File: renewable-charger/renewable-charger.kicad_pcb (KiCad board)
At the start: 2 copper layers, 149.9 x 41.9 mm, 31 parts, among them J1 Solar Input, J2 Wind Output, J3 Output, M1 Stepper_Motor_bipolar, Q1 P-channel 30V 4A MOSfet, U1 CN3791

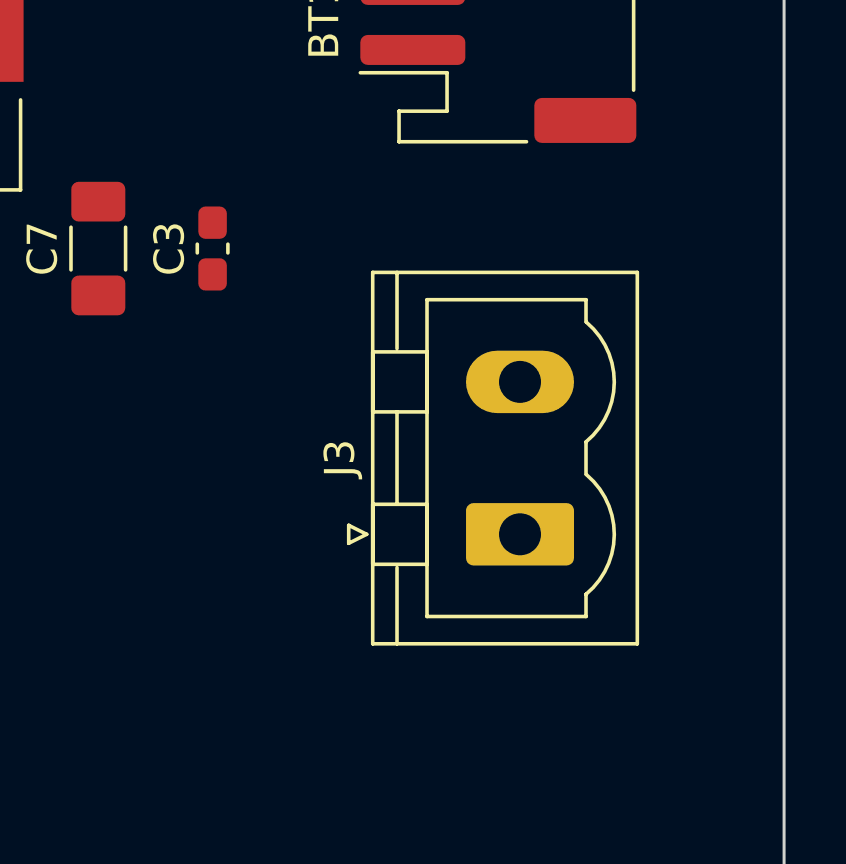
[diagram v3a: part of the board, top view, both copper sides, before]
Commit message: Add test point to measure current into the battery.  Implements #8
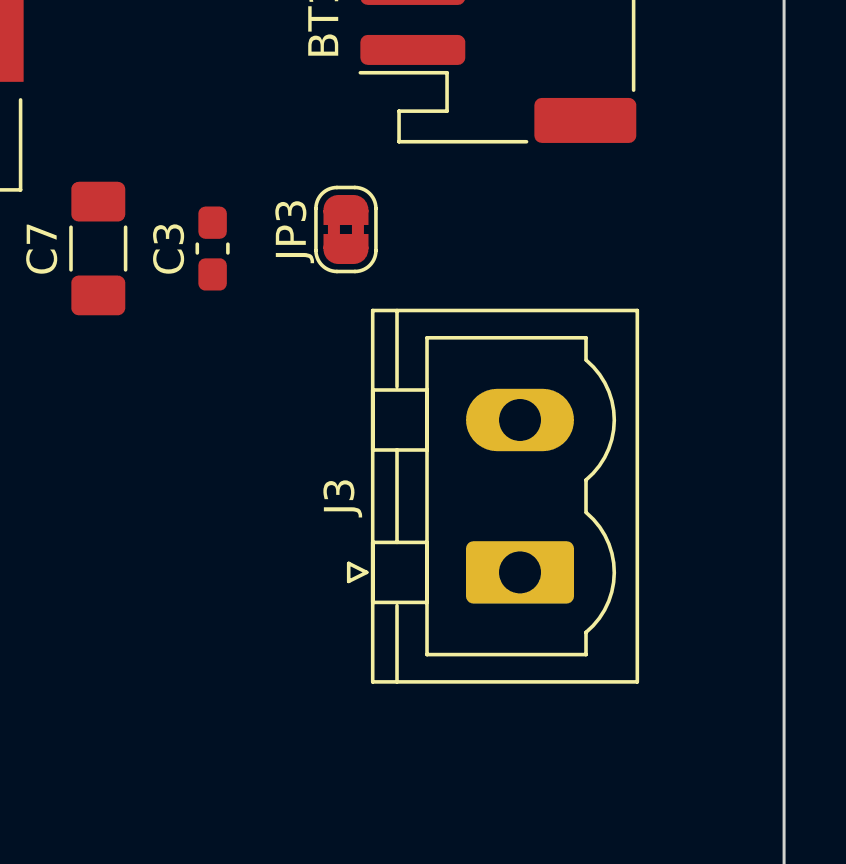
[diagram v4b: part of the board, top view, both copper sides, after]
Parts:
- added JP3: Test Point, Jumper:SolderJumper-2_P1.3mm_Bridged2Bar_RoundedPad1.0x1.5mm, F.Cu at (247.7, 77.5)
- moved J3 1.27 mm to (253.5, 88.9)
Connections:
- C3 pad 1: Net-(BT1-+) -> Net-(J3-Pin_1)
- C7 pad 1: Net-(BT1-+) -> Net-(J3-Pin_1)
- J3 pad 1: Net-(BT1-+) -> Net-(J3-Pin_1)
- R5 pad 2: Net-(BT1-+) -> Net-(J3-Pin_1)
- U1 pad 7: Net-(BT1-+) -> Net-(J3-Pin_1)
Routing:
- net Net-(J3-Pin_1): track 0.00 -> 14.2 mm
- net Net-(BT1-+): track 14.2 -> 0.00 mm
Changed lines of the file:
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@@
   (net 19 "Net-(M1--)")
   (net 20 "Net-(JP2-A)")
+  (net 21 "Net-(J3-Pin_1)")
   (footprint "Resistor_SMD:R_0805_2012Metric_Pad1.20x1.40mm_HandSolder" (layer "F.Cu")
     (at 230.505 78.74 -90)
@@
       (net 11 "Net-(U1-CSP)") (pintype "passive"))
     (pad "2" smd roundrect (at 1 0 270) (size 1.2 1.4) (layers "F.Cu" "F.Paste" "F.Mask") (roundrect_rratio 0.208333)
-      (net 1 "Net-(BT1-+)") (pintype "passive"))
+      (net 21 "Net-(J3-Pin_1)") (pintype "passive"))
     (model "${KICAD6_3DMODEL_DIR}/Resistor_SMD.3dshapes/R_0805_2012Metric.wrl"
       (offset (xyz 0 0 0))
@@
   )
   (footprint "Connector_Phoenix_MSTB:PhoenixContact_MSTBVA_2,5_2-G-5,08_1x02_P5.08mm_Vertical" (layer "F.Cu")
-    (at 253.4525 87.63 90)
+    (at 253.4525 88.9 90)
     (descr "Generic Phoenix Contact connector footprint for: MSTBVA_2,5/2-G-5,08; number of pins: 02; pin pitch: 5.08mm; Vertical || order number: 1755736 12A || order number: 1924305 16A (HC)")
     (tags "phoenix_contact connector MSTBVA_01x02_G_5.08mm")
@@
       (stroke (width 0.1) (type solid)) (layer "F.Fab"))
     (pad "1" thru_hole roundrect (at 0 0 90) (size 2.08 3.6) (drill 1.4) (layers *.Cu *.Mask) (roundrect_rratio 0.120192)
-      (net 1 "Net-(BT1-+)") (pinfunction "Pin_1") (pintype "passive"))
+      (net 21 "Net-(J3-Pin_1)") (pinfunction "Pin_1") (pintype "passive"))
     (pad "2" thru_hole oval (at 5.08 0 90) (size 2.08 3.6) (drill 1.4) (layers *.Cu *.Mask)
       (net 2 "/Power -") (pinfunction "Pin_2") (pintype "passive"))
@@
       (stroke (width 0.1) (type solid)) (layer "F.Fab"))
     (pad "1" smd roundrect (at -0.8625 0 90) (size 1.075 0.95) (layers "F.Cu" "F.Paste" "F.Mask") (roundrect_rratio 0.25)
-      (net 1 "Net-(BT1-+)") (pintype "passive"))
+      (net 21 "Net-(J3-Pin_1)") (pintype "passive"))
     (pad "2" smd roundrect (at 0.8625 0 90) (size 1.075 0.95) (layers "F.Cu" "F.Paste" "F.Mask") (roundrect_rratio 0.25)
       (net 2 "/Power -") (pintype "passive"))
@@
     )
   )
+  (footprint "Jumper:SolderJumper-2_P1.3mm_Bridged2Bar_RoundedPad1.0x1.5mm" (layer "F.Cu")
+    (at 247.65 77.47 90)
+    (descr "SMD Solder Jumper, 1x1.5mm, rounded Pads, 0.3mm gap, bridged with 2 copper strips")
+    (tags "net tie solder jumper bridged")
+    (property "Sheetfile" "renewable-charger.kicad_sch")
+    (property "Sheetname" "")
+    (attr exclude_from_pos_files)
+    (fp_text reference "JP3" (at 0 -1.8 90) (layer "F.SilkS")
+      (effects (font (size 1 1) (thickness 0.15)))
+    )
+    (fp_text value "Test Point" (at 0 1.9 90) (layer "F.Fab")
+      (effects (font (size 1 1) (thickness 0.15)))
+    )
+    (fp_poly
+      (pts
+        (xy -0.25 -0.6)
+        (xy 0.25 -0.6)
+        (xy 0.25 -0.2)
+        (xy -0.25 -0.2)
+      )
+      (stroke (width 0) (type solid)) (fill solid) (layer "F.Cu"))
+    (fp_poly
+      (pts
+        (xy -0.25 0.2)
+        (xy 0.25 0.2)
+        (xy 0.25 0.6)
+        (xy -0.25 0.6)
+      )
+      (stroke (width 0) (type solid)) (fill solid) (layer "F.Cu"))
+    (fp_line (start -1.4 0.3) (end -1.4 -0.3)
+      (stroke (width 0.12) (type solid)) (layer "F.SilkS"))
+    (fp_line (start -0.7 -1) (end 0.7 -1)
+      (stroke (width 0.12) (type solid)) (layer "F.SilkS"))
+    (fp_line (start 0.7 1) (end -0.7 1)
+      (stroke (width 0.12) (type solid)) (layer "F.SilkS"))
+    (fp_line (start 1.4 -0.3) (end 1.4 0.3)
+      (stroke (width 0.12) (type solid)) (layer "F.SilkS"))
+    (fp_arc (start -1.4 -0.3) (mid -1.194975 -0.794975) (end -0.7 -1)
+      (stroke (width 0.12) (type solid)) (layer "F.SilkS"))
+    (fp_arc (start -0.7 1) (mid -1.194975 0.794975) (end -1.4 0.3)
+      (stroke (width 0.12) (type solid)) (layer "F.SilkS"))
+    (fp_arc (start 0.7 -1) (mid 1.194975 -0.794975) (end 1.4 -0.3)
+      (stroke (width 0.12) (type solid)) (layer "F.SilkS"))
+    (fp_arc (start 1.4 0.3) (mid 1.194975 0.794975) (end 0.7 1)
+      (stroke (width 0.12) (type solid)) (layer "F.SilkS"))
+    (fp_line (start -1.65 -1.25) (end -1.65 1.25)
+      (stroke (width 0.05) (type solid)) (layer "F.CrtYd"))
+    (fp_line (start -1.65 -1.25) (end 1.65 -1.25)
+      (stroke (width 0.05) (type solid)) (layer "F.CrtYd"))
+    (fp_line (start 1.65 1.25) (end -1.65 1.25)
+      (stroke (width 0.05) (type solid)) (layer "F.CrtYd"))
+    (fp_line (start 1.65 1.25) (end 1.65 -1.25)
+      (stroke (width 0.05) (type solid)) (layer "F.CrtYd"))
+    (pad "1" smd custom (at -0.65 0 90) (size 1 0.5) (layers "F.Cu" "F.Mask")
+      (net 21 "Net-(J3-Pin_1)") (pinfunction "A") (pintype "passive") (zone_connect 2) (thermal_bridge_angle 45)
+      (options (clearance outline) (anchor rect))
+      (primitives
+        (gr_circle (center 0 0.25) (end 0.5 0.25) (width 0) (fill yes))
+        (gr_circle (center 0 -0.25) (end 0.5 -0.25) (width 0) (fill yes))
+        (gr_poly
+          (pts
+            (xy 0.5 0.75)
+            (xy 0 0.75)
+            (xy 0 -0.75)
+            (xy 0.5 -0.75)
+          )
+ (width 0) (fill yes))
+      ))
+    (pad "2" smd custom (at 0.65 0 90) (size 1 0.5) (layers "F.Cu" "F.Mask")
+      (net 1 "Net-(BT1-+)") (pinfunction "B") (pintype "passive") (zone_connect 2) (thermal_bridge_angle 45)
+      (options (clearance outline) (anchor rect))
+      (primitives
+        (gr_circle (center 0 0.25) (end 0.5 0.25) (width 0) (fill yes))
+        (gr_circle (center 0 -0.25) (end 0.5 -0.25) (width 0) (fill yes))
+        (gr_poly
+          (pts
+            (xy 0 0.75)
+            (xy -0.5 0.75)
+            (xy -0.5 -0.75)
+            (xy 0 -0.75)
+          )
+ (width 0) (fill yes))
+      ))
+  )
   (footprint "Package_TO_SOT_SMD:SOT-23" (layer "F.Cu")
     (at 209.55 70.485)
@@
       (stroke (width 0.1) (type solid)) (layer "F.Fab"))
     (pad "1" smd roundrect (at -1.5625 0 90) (size 1.325 1.8) (layers "F.Cu" "F.Paste" "F.Mask") (roundrect_rratio 0.188679)
-      (net 1 "Net-(BT1-+)") (pintype "passive"))
+      (net 21 "Net-(J3-Pin_1)") (pintype "passive"))
     (pad "2" smd roundrect (at 1.5625 0 90) (size 1.325 1.8) (layers "F.Cu" "F.Paste" "F.Mask") (roundrect_rratio 0.188679)
       (net 2 "/Power -") (pintype "passive"))
@@
       (net 14 "Net-(U1-MPPT)") (pinfunction "MPPT") (pintype "input"))
     (pad "7" smd rect (at 2.55 1 90) (size 1.1 0.51) (layers "F.Cu" "F.Paste" "F.Mask")
-      (net 1 "Net-(BT1-+)") (pinfunction "BAT") (pintype "input"))
+      (net 21 "Net-(J3-Pin_1)") (pinfunction "BAT") (pintype "input"))
     (pad "8" smd rect (at 2.55 0 90) (size 1.1 0.51) (layers "F.Cu" "F.Paste" "F.Mask")
       (net 11 "Net-(U1-CSP)") (pinfunction "CSP") (pintype "input"))
@@
   (gr_rect (start 112.395 59.69) (end 262.255 101.6)
     (stroke (width 0.1) (type default)) (fill none) (layer "Edge.Cuts"))
-  (segment (start 219.44 76.19) (end 219.44 75.895) (width 0.25) (layer "F.Cu") (net 1))
-  (segment (start 221.364771 75.315489) (end 224.155 78.105718) (width 0.25) (layer "F.Cu") (net 1))
-  (segment (start 224.155 79.375) (end 224.52 79.74) (width 0.25) (layer "F.Cu") (net 1))
-  (segment (start 224.155 78.105718) (end 224.155 79.375) (width 0.25) (layer "F.Cu") (net 1))
-  (segment (start 220.019511 75.315489) (end 221.364771 75.315489) (width 0.25) (layer "F.Cu") (net 1))
-  (segment (start 224.52 79.74) (end 230.505 79.74) (width 0.25) (layer "F.Cu") (net 1))
-  (segment (start 219.44 75.895) (end 220.019511 75.315489) (width 0.25) (layer "F.Cu") (net 1))
   (segment (start 168.8 83.82) (end 168.8 75.04) (width 1.3) (layer "F.Cu") (net 2))
   (segment (start 129.06 71.91) (end 125.79 71.91) (width 1.3) (layer "F.Cu") (net 2))
@@
   (segment (start 163.195 67.31) (end 163.1075 67.2225) (width 0.25) (layer "F.Cu") (net 20))
   (segment (start 163.195 75.55) (end 163.195 67.31) (width 0.25) (layer "F.Cu") (net 20))
+  (segment (start 219.44 76.19) (end 219.44 75.895) (width 0.25) (layer "F.Cu") (net 21))
+  (segment (start 221.364771 75.315489) (end 224.155 78.105718) (width 0.25) (layer "F.Cu") (net 21))
+  (segment (start 224.155 79.375) (end 224.52 79.74) (width 0.25) (layer "F.Cu") (net 21))
+  (segment (start 224.155 78.105718) (end 224.155 79.375) (width 0.25) (layer "F.Cu") (net 21))
+  (segment (start 220.019511 75.315489) (end 221.364771 75.315489) (width 0.25) (layer "F.Cu") (net 21))
+  (segment (start 224.52 79.74) (end 230.505 79.74) (width 0.25) (layer "F.Cu") (net 21))
+  (segment (start 219.44 75.895) (end 220.019511 75.315489) (width 0.25) (layer "F.Cu") (net 21))
 )

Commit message: Add micro-USB connector for USB charging.  Implements #7
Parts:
- added J4: USB_B_Micro, Connector_USB:USB_Micro-B_Amphenol_10118194_Horizontal, F.Cu at (193.0, 89.5)
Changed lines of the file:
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@@
   (net 20 "Net-(JP2-A)")
   (net 21 "Net-(J3-Pin_1)")
+  (net 22 "unconnected-(J4-D-)")
+  (net 23 "unconnected-(J4-D+)")
+  (net 24 "unconnected-(J4-ID)")
+  (net 25 "unconnected-(J4-Shield)")
   (footprint "Resistor_SMD:R_0805_2012Metric_Pad1.20x1.40mm_HandSolder" (layer "F.Cu")
     (at 230.505 78.74 -90)
@@
       (offset (xyz 0 0 0))
       (scale (xyz 1 1 1))
+      (rotate (xyz 0 0 0))
+    )
+  )
+  (footprint "Connector_USB:USB_Micro-B_Amphenol_10118194_Horizontal" (layer "F.Cu")
+    (at 193.04 89.535)
+    (descr "USB Micro-B receptacle, horizontal, SMD, 10118194, https://cdn.amphenol-icc.com/media/wysiwyg/files/drawing/10118194.pdf")
+    (tags "USB Micro B horizontal SMD")
+    (property "Farnell" "2668482")
+    (property "Farnell Price/Stock" "https://uk.farnell.com/amphenol-icc-fci/10118194-0001lf/micro-usb-2-0-type-b-rcpt-smt/dp/2668482")
+    (property "Sheetfile" "renewable-charger.kicad_sch")
+    (property "Sheetname" "")
+    (attr smd)
+    (fp_text reference "J4" (at 0 -3.5) (layer "F.SilkS")
+      (effects (font (size 1 1) (thickness 0.15)))
+    )
+    (fp_text value "USB_B_Micro" (at 0 4.75) (layer "F.Fab")
+      (effects (font (size 1 1) (thickness 0.15)))
+    )
+    (fp_text user "PCB Edge" (at 0 2.75) (layer "Dwgs.User")
+      (effects (font (size 0.5 0.5) (thickness 0.08)))
+    )
+    (fp_text user "${REFERENCE}" (at 0 -0.05) (layer "F.Fab")
+      (effects (font (size 1 1) (thickness 0.15)))
+    )
+    (fp_line (start -3.76 -1.66) (end -3.34 -1.66)
+      (stroke (width 0.12) (type solid)) (layer "F.SilkS"))
+    (fp_line (start -3.76 0.32) (end -3.76 -1.66)
+      (stroke (width 0.12) (type solid)) (layer "F.SilkS"))
+    (fp_line (start -3.76 2.69) (end -3.76 2.29)
+      (stroke (width 0.12) (type solid)) (layer "F.SilkS"))
+    (fp_line (start -1.76 -1.89) (end -1.76 -2.34)
+      (stroke (width 0.12) (type solid)) (layer "F.SilkS"))
+    (fp_line (start -1.31 -2.34) (end -1.76 -2.34)
+      (stroke (width 0.12) (type solid)) (layer "F.SilkS"))
+    (fp_line (start 3.76 -1.66) (end 3.34 -1.66)
+      (stroke (width 0.12) (type solid)) (layer "F.SilkS"))
+    (fp_line (start 3.76 0.32) (end 3.76 -1.66)
+      (stroke (width 0.12) (type solid)) (layer "F.SilkS"))
+    (fp_line (start 3.76 2.29) (end 3.76 2.69)
+      (stroke (width 0.12) (type solid)) (layer "F.SilkS"))
+    (fp_line (start 3 2.75) (end -3 2.75)
+      (stroke (width 0.1) (type solid)) (layer "Dwgs.User"))
+    (fp_line (start -4.45 -2.58) (end -4.45 3.95)
+      (stroke (width 0.05) (type solid)) (layer "F.CrtYd"))
+    (fp_line (start -4.45 -2.58) (end 4.45 -2.58)
+      (stroke (width 0.05) (type solid)) (layer "F.CrtYd"))
+    (fp_line (start -4.45 3.95) (end 4.45 3.95)
+      (stroke (width 0.05) (type solid)) (layer "F.CrtYd"))
+    (fp_line (start 4.45 -2.58) (end 4.45 3.95)
+      (stroke (width 0.05) (type solid)) (layer "F.CrtYd"))
+    (fp_line (start -3.65 -0.55) (end -2.65 -1.55)
+      (stroke (width 0.1) (type solid)) (layer "F.Fab"))
+    (fp_line (start -3.65 3.45) (end -3.65 -0.55)
+      (stroke (width 0.1) (type solid)) (layer "F.Fab"))
+    (fp_line (start -2.65 -1.55) (end 3.65 -1.55)
+      (stroke (width 0.1) (type solid)) (layer "F.Fab"))
+    (fp_line (start 3.65 -1.55) (end 3.65 3.45)
+      (stroke (width 0.1) (type solid)) (layer "F.Fab"))
+    (fp_line (start 3.65 3.45) (end -3.65 3.45)
+      (stroke (width 0.1) (type solid)) (layer "F.Fab"))
+    (pad "" smd oval (at -3.5 1.3) (size 0.89 1.55) (layers "F.Paste"))
+    (pad "" smd oval (at -2.5 -1.4) (size 1.25 0.95) (layers "F.Paste"))
+    (pad "" smd oval (at 2.5 -1.4) (size 1.25 0.95) (layers "F.Paste"))
+    (pad "" smd oval (at 3.5 1.3) (size 0.89 1.55) (layers "F.Paste"))
+    (pad "1" smd rect (at -1.3 -1.4) (size 0.4 1.35) (layers "F.Cu" "F.Paste" "F.Mask")
+      (net 3 "/Power +") (pinfunction "VBUS") (pintype "power_out"))
+    (pad "2" smd rect (at -0.65 -1.4) (size 0.4 1.35) (layers "F.Cu" "F.Paste" "F.Mask")
+      (net 22 "unconnected-(J4-D-)") (pinfunction "D-") (pintype "bidirectional+no_connect"))
+    (pad "3" smd rect (at 0 -1.4) (size 0.4 1.35) (layers "F.Cu" "F.Paste" "F.Mask")
+      (net 23 "unconnected-(J4-D+)") (pinfunction "D+") (pintype "bidirectional+no_connect"))
+    (pad "4" smd rect (at 0.65 -1.4) (size 0.4 1.35) (layers "F.Cu" "F.Paste" "F.Mask")
+      (net 24 "unconnected-(J4-ID)") (pinfunction "ID") (pintype "passive+no_connect"))
+    (pad "5" smd rect (at 1.3 -1.4) (size 0.4 1.35) (layers "F.Cu" "F.Paste" "F.Mask")
+      (net 2 "/Power -") (pinfunction "GND") (pintype "power_out"))
+    (pad "6" thru_hole oval (at -3.5 1.3) (size 0.89 1.55) (drill oval 0.5 1.15) (layers *.Cu *.Mask)
+      (net 25 "unconnected-(J4-Shield)") (pinfunction "Shield") (pintype "passive+no_connect"))
+    (pad "6" smd rect (at -2.9 1.3) (size 1.2 1.55) (layers "F.Cu" "F.Paste" "F.Mask")
+      (net 25 "unconnected-(J4-Shield)") (pinfunction "Shield") (pintype "passive+no_connect"))
+    (pad "6" thru_hole oval (at -2.5 -1.4) (size 1.25 0.95) (drill oval 0.85 0.55) (layers *.Cu *.Mask)
+      (net 25 "unconnected-(J4-Shield)") (pinfunction "Shield") (pintype "passive+no_connect"))
+    (pad "6" smd rect (at -1 1.3) (size 1.5 1.55) (layers "F.Cu" "F.Paste" "F.Mask")
+      (net 25 "unconnected-(J4-Shield)") (pinfunction "Shield") (pintype "passive+no_connect"))
+    (pad "6" smd rect (at 1 1.3) (size 1.5 1.55) (layers "F.Cu" "F.Paste" "F.Mask")
+      (net 25 "unconnected-(J4-Shield)") (pinfunction "Shield") (pintype "passive+no_connect"))
+    (pad "6" thru_hole oval (at 2.5 -1.4) (size 1.25 0.95) (drill oval 0.85 0.55) (layers *.Cu *.Mask)
+      (net 25 "unconnected-(J4-Shield)") (pinfunction "Shield") (pintype "passive+no_connect"))
+    (pad "6" smd rect (at 2.9 1.3) (size 1.2 1.55) (layers "F.Cu" "F.Paste" "F.Mask")
+      (net 25 "unconnected-(J4-Shield)") (pinfunction "Shield") (pintype "passive+no_connect"))
+    (pad "6" thru_hole oval (at 3.5 1.3) (size 0.89 1.55) (drill oval 0.5 1.15) (layers *.Cu *.Mask)
+      (net 25 "unconnected-(J4-Shield)") (pinfunction "Shield") (pintype "passive+no_connect"))
+    (model "${KICAD6_3DMODEL_DIR}/Connector_USB.3dshapes/USB_Micro-B_Amphenol_10118194_Horizontal.wrl"
+      (offset (xyz 0 0 0))
+      (scale (xyz 1 1 1))

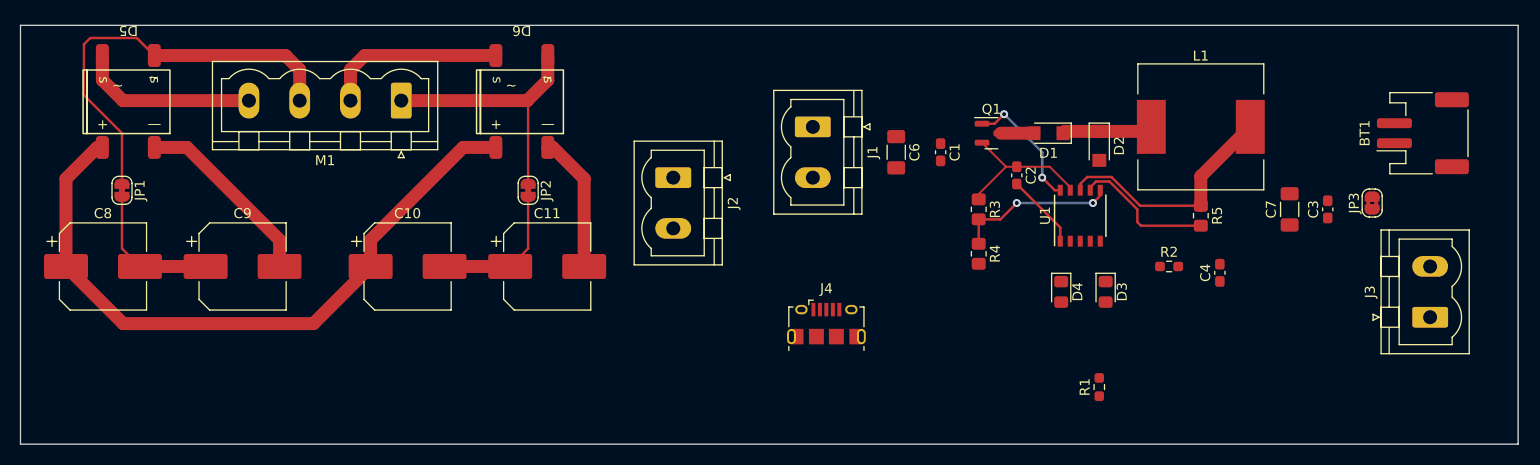
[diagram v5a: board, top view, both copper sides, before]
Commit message: Reduce power trace thickness
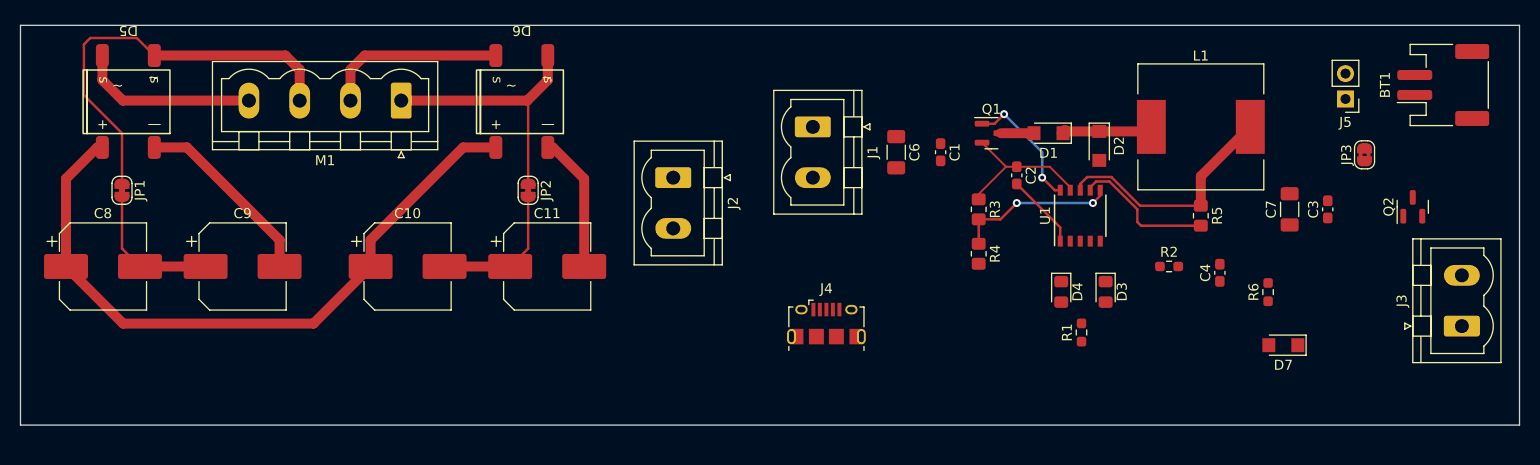
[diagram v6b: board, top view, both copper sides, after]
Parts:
- added D7: D_Schottky, Diode_SMD:D_SMF, F.Cu at (238.8, 91.7)
- added J5: Battery, Connector_PinHeader_2.54mm:PinHeader_1x02_P2.54mm_Vertical, F.Cu at (245.0, 67.1)
- added Q2: P-channel 30V 4A MOSfet, Package_TO_SOT_SMD:SOT-23, F.Cu at (251.7, 77.9)
- added R6: R_Small, Resistor_SMD:R_0603_1608Metric_Pad0.98x0.95mm_HandSolder, F.Cu at (237.2, 86.4)
- D1, D2: value D_Zener -> D_Schottky
- moved R1 5.74 mm to (218.6, 90.4)
- moved BT1 5.24 mm to (254.8, 65.7)
- moved JP3 4.89 mm to (246.9, 72.6)
- moved J3 3.30 mm to (256.6, 89.8)
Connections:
- C3 pad 1: Net-(J3-Pin_1) -> Net-(JP3-A)
- C7 pad 1: Net-(J3-Pin_1) -> Net-(JP3-A)
- J3 pad 1: Net-(J3-Pin_1) -> Net-(D7-K)
- JP3 pad 1: Net-(J3-Pin_1) -> Net-(JP3-A)
- R5 pad 2: Net-(J3-Pin_1) -> Net-(JP3-A)
- U1 pad 7: Net-(J3-Pin_1) -> Net-(JP3-A)
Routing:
- net Net-(JP3-A): track 0.00 -> 14.2 mm
- net Net-(J3-Pin_1): track 14.2 -> 0.00 mm
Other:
- board size 149.9 x 41.9 mm -> 150 x 40 mm
